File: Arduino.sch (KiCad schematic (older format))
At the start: 0 parts

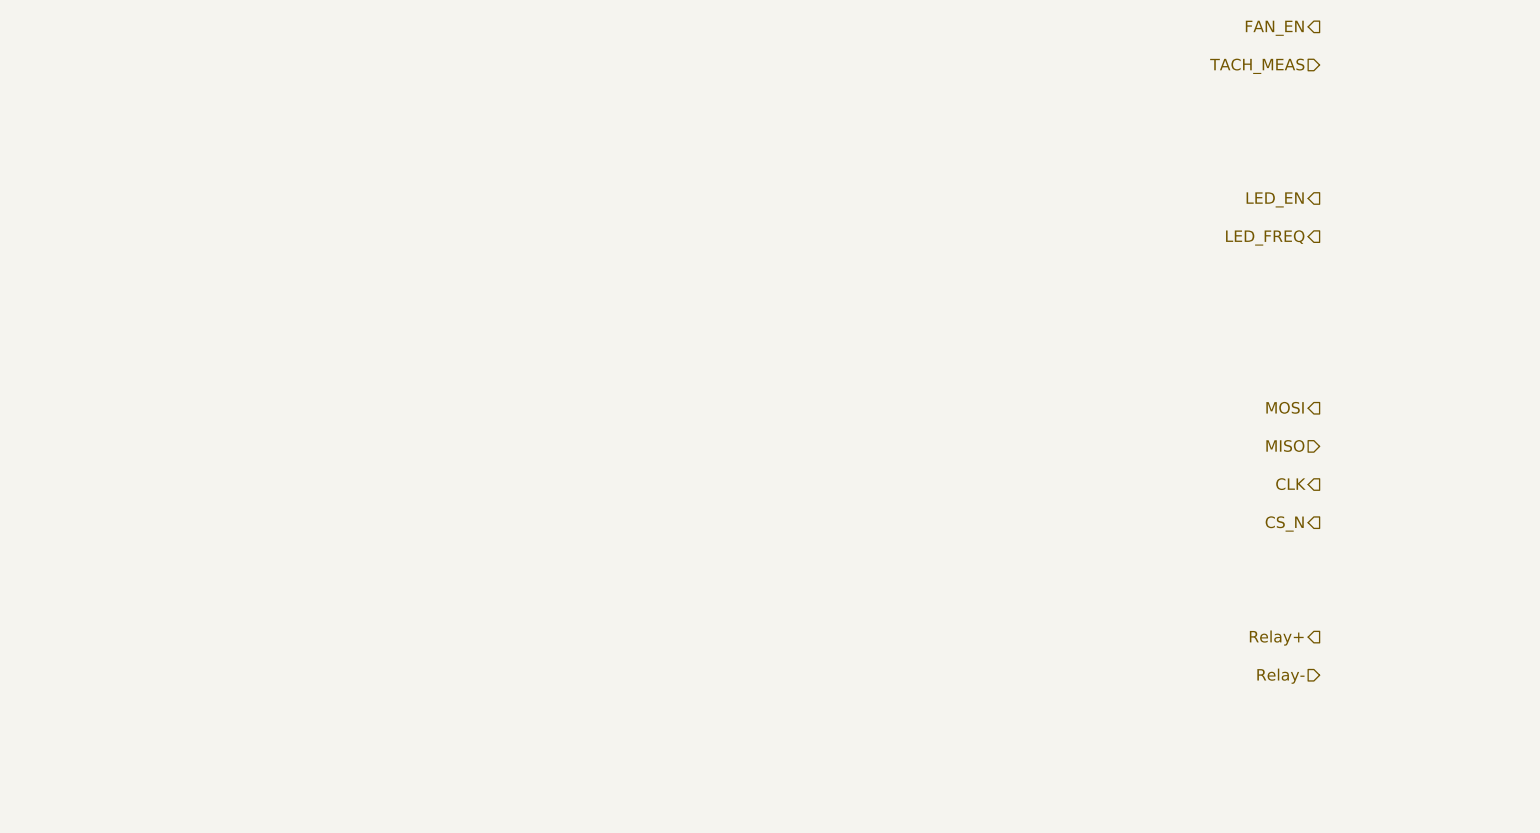
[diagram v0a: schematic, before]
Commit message: Added Arduino and top-level connections
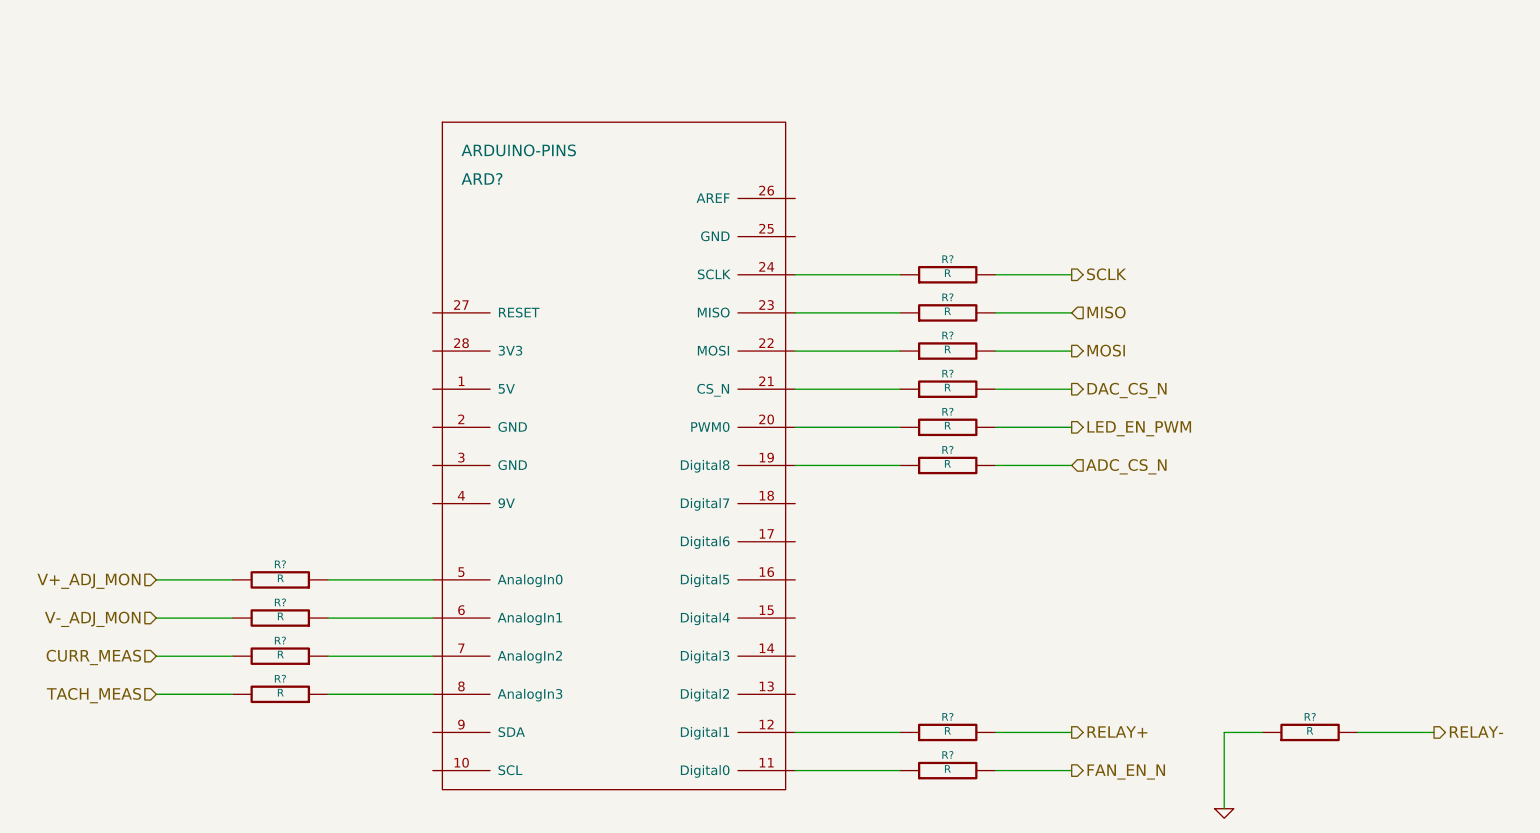
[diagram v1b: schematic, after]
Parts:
- added ARD?: ARDUINO-PINS, symbol ARDUINO-PINS
- added R? (x13): R, symbol R
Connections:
- net MISO: now also R?.2
- net MOSI: now also R?.2
- net TACH_MEAS: now also R?.2
- new net: ARD?.11 (Digital0), R?.1
- new net: ARD?.12 (Digital1), R?.1
- new net: ARD?.19 (Digital8), R?.1
- new net: ARD?.20 (PWM0), R?.1
- new net: ARD?.21 (CS_N), R?.1
- new net: ARD?.22 (MOSI), R?.1
- new net: ARD?.23 (MISO), R?.1
- new net: ARD?.24 (SCLK), R?.1
- new net: ARD?.5 (AnalogIn0), R?.1
- new net: ARD?.6 (AnalogIn1), R?.1
- new net: ARD?.7 (AnalogIn2), R?.1
- new net: ARD?.8 (AnalogIn3), R?.1
- new net ADC_CS_N: R?.2
- new net CURR_MEAS: R?.2
- new net DAC_CS_N: R?.2
- new net FAN_EN_N: R?.2
- new net GND: R?.1
- new net LED_EN_PWM: R?.2
- new net RELAY+: R?.2
- new net RELAY-: R?.2
- new net SCLK: R?.2
- new net V+_ADJ_MON: R?.2
- new net V-_ADJ_MON: R?.2

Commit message: Some cleanup/fixes on the top-level
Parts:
- added R? (x2): R, symbol R
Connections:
- net at ARD?.11 (Digital0): now also R?.1; no longer R?.1
- net at ARD?.18 (Digital7): now also R?.1
- net at ARD?.21 (CS_N): now also R?.1; no longer R?.1
- net at ARD?.4 (9V): now also R?.1
- net FAN_EN_N renamed FAN_PWM
- new net +12P: R?.2
- new net FAN_MODE: R?.2
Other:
- moved on the sheet: R?
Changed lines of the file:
@@
 $Descr A4 11693 8268
 encoding utf-8
-Sheet 7 9
+Sheet 9 9
 Title ""
 Date ""
@@
 Text HLabel 7100 2800 2    60   Output ~ 0
 SCLK
+Text HLabel 7100 4000 2    60   Output ~ 0
+DAC_CS_N
 Text HLabel 7100 3400 2    60   Output ~ 0
-DAC_CS_N
-Text HLabel 7100 5400 2    60   Output ~ 0
-FAN_EN_N
+FAN_PWM
 Text HLabel 2300 5000 0    60   Input ~ 0
 TACH_MEAS
@@
 L R R?
 U 1 1 52FC2526
-P 6450 5400
-F 0 "R?" V 6530 5400 40  0000 C CNN
-F 1 "R" V 6457 5401 40  0000 C CNN
-F 2 "" V 6380 5400 30  0000 C CNN
-F 3 "" H 6450 5400 30  0000 C CNN
-	1    6450 5400
-	0    -1   -1   0
-$EndComp
-Wire Wire Line
-	6700 5400 7100 5400
+P 6450 3400
+F 0 "R?" V 6530 3400 40  0000 C CNN
+F 1 "R" V 6457 3401 40  0000 C CNN
+F 2 "" V 6380 3400 30  0000 C CNN
+F 3 "" H 6450 3400 30  0000 C CNN
+	1    6450 3400
+	0    -1   -1   0
+$EndComp
+Wire Wire Line
+	6700 3400 7100 3400
 $Comp
 L R R?
@@
 	6200 5200 5650 5200
 Wire Wire Line
-	5650 5400 6200 5400
+	5650 3400 6200 3400
 $Comp
 L R R?
@@
 L R R?
 U 1 1 52FC406F
-P 6450 3400
-F 0 "R?" V 6530 3400 40  0000 C CNN
-F 1 "R" V 6457 3401 40  0000 C CNN
-F 2 "" V 6380 3400 30  0000 C CNN
-F 3 "" H 6450 3400 30  0000 C CNN
-	1    6450 3400
-	0    -1   -1   0
-$EndComp
-Wire Wire Line
-	6700 3400 7100 3400
+P 6450 4000
+F 0 "R?" V 6530 4000 40  0000 C CNN
+F 1 "R" V 6457 4001 40  0000 C CNN
+F 2 "" V 6380 4000 30  0000 C CNN
+F 3 "" H 6450 4000 30  0000 C CNN
+	1    6450 4000
+	0    -1   -1   0
+$EndComp
+Wire Wire Line
+	6700 4000 7100 4000
 $Comp
 L R R?
@@
 	6200 3200 5650 3200
 Wire Wire Line
-	5650 3400 6200 3400
+	5650 4000 6200 4000
 $Comp
 L R R?
@@
 Wire Wire Line
 	5650 3800 6200 3800
+Text HLabel 7100 5400 2    60   Input ~ 0
+FAN_MODE
+$Comp
+L R R?
+U 1 1 52FC1D68
+P 6450 5400
+F 0 "R?" V 6530 5400 40  0000 C CNN
+F 1 "R" V 6457 5401 40  0000 C CNN
+F 2 "" V 6380 5400 30  0000 C CNN
+F 3 "" H 6450 5400 30  0000 C CNN
+	1    6450 5400
+	0    -1   -1   0
+$EndComp
+Wire Wire Line
+	6700 5400 7100 5400
+Wire Wire Line
+	6200 5400 5650 5400
+$Comp
+L R R?
+U 1 1 52FC23F0
+P 2950 4000
+F 0 "R?" V 3030 4000 40  0000 C CNN
+F 1 "R" V 2957 4001 40  0000 C CNN
+F 2 "" V 2880 4000 30  0000 C CNN
+F 3 "" H 2950 4000 30  0000 C CNN
+	1    2950 4000
+	0    1    -1   0
+$EndComp
+Wire Wire Line
+	2700 4000 2300 4000
+Wire Wire Line
+	3200 4000 3750 4000
+$Comp
+L +12P #PWR?
+U 1 1 52FC23FA
+P 2300 3800
+F 0 "#PWR?" H 2300 3770 30  0001 C CNN
+F 1 "+12P" H 2300 3900 30  0000 C CNN
+F 2 "" H 2300 3800 60  0000 C CNN
+F 3 "" H 2300 3800 60  0000 C CNN
+	1    2300 3800
+	1    0    0    -1
+$EndComp
+Wire Wire Line
+	2300 4000 2300 3800
 $EndSCHEMATC

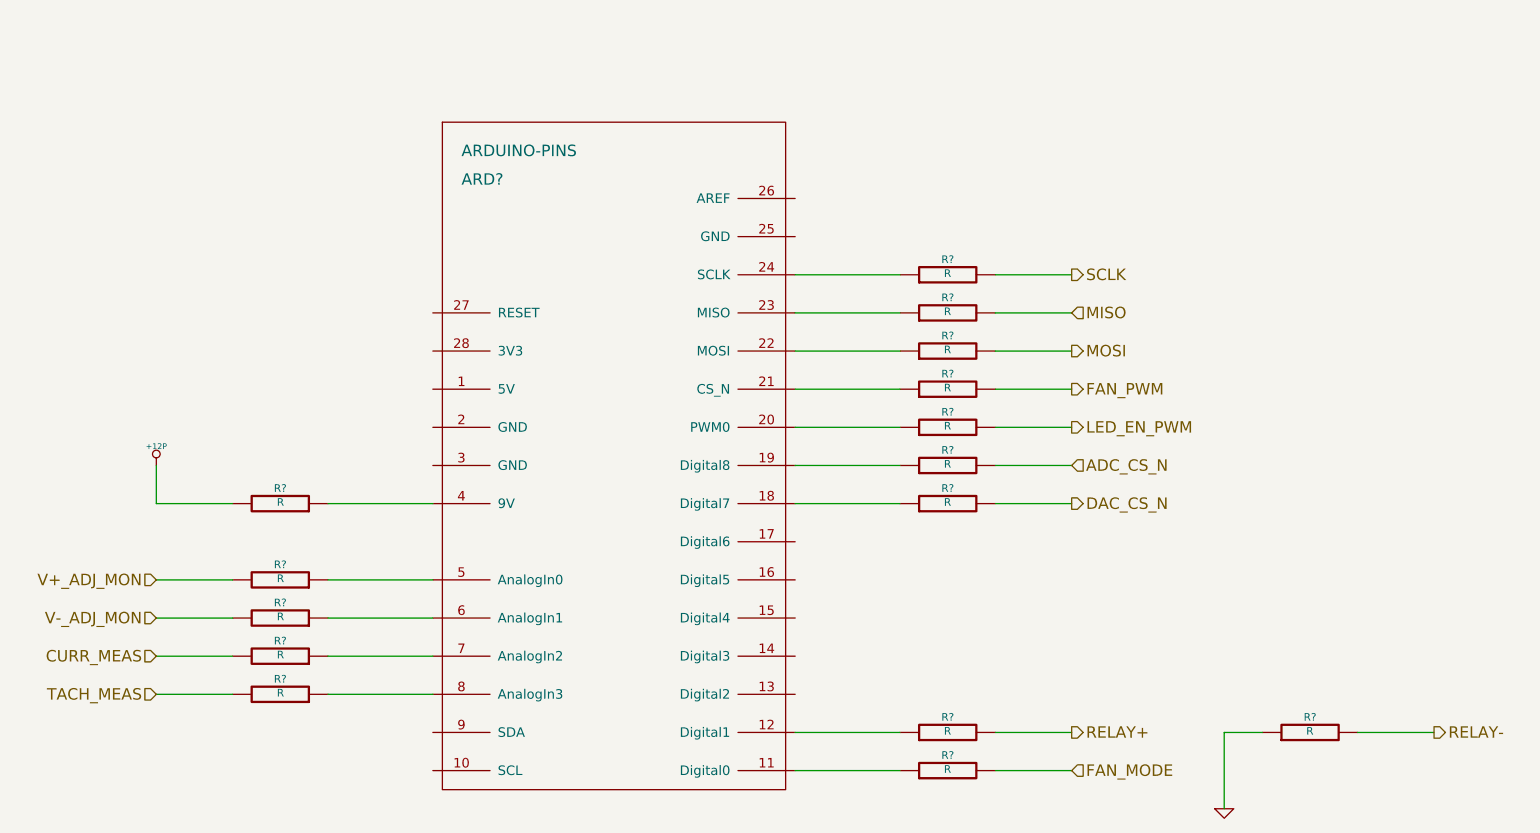
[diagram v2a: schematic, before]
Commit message: Added footprints for the relay module, preliminarily annotated schematic, relay components placed on PCB
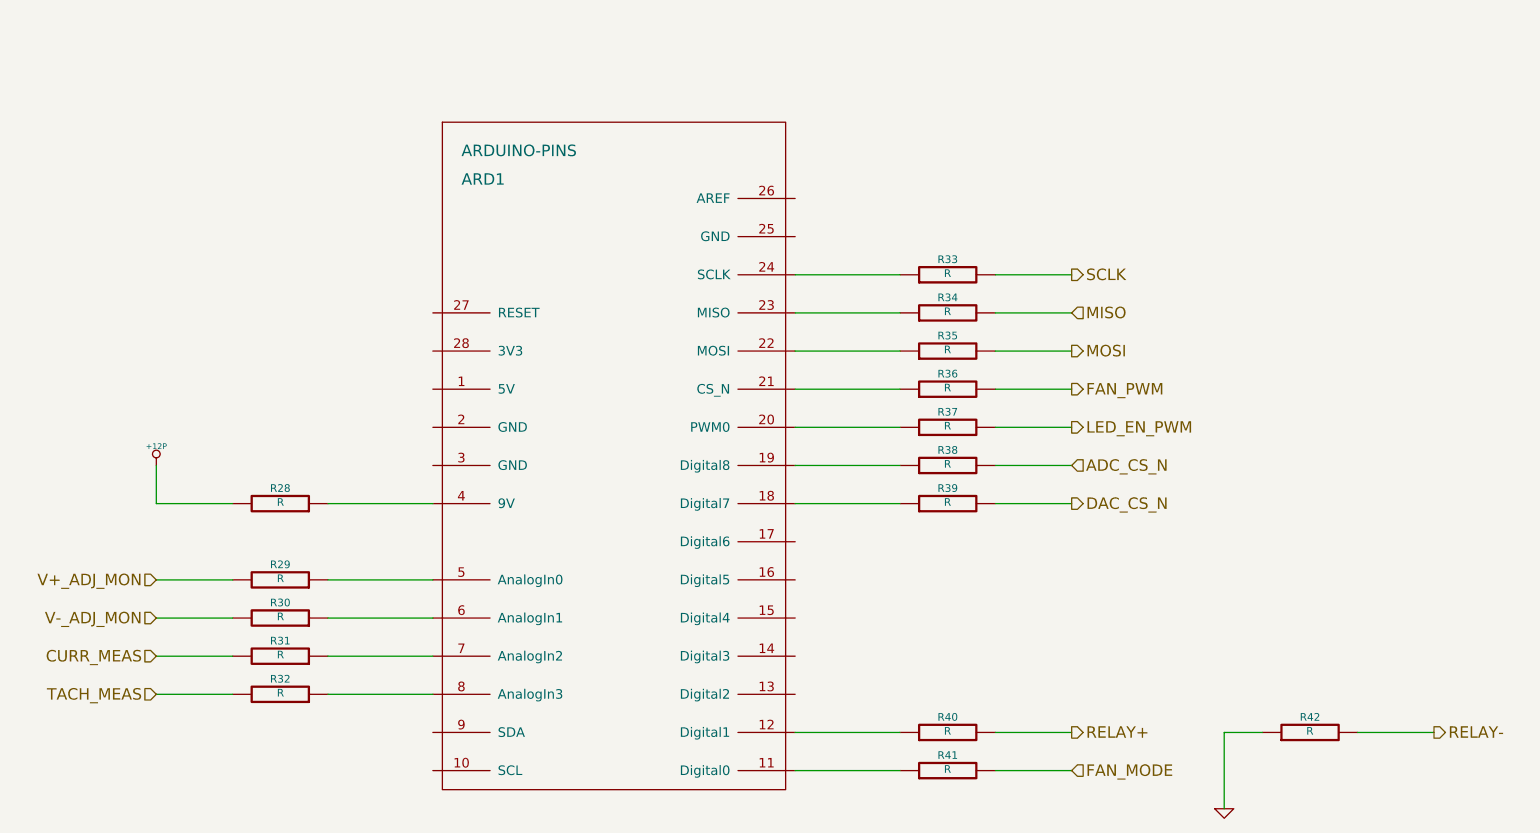
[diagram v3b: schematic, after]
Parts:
- gave numbers to parts that had none: 16
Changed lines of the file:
@@
 TACH_MEAS
 $Comp
-L ARDUINO-PINS ARD?
+L ARDUINO-PINS ARD1
 U 1 1 52FC2370
 P 4700 4100
-F 0 "ARD?" H 3900 5900 60  0000 L CNN
+F 0 "ARD1" H 3900 5900 60  0000 L CNN
 F 1 "ARDUINO-PINS" H 3900 6050 60  0000 L CNN
 F 2 "" H 4700 4100 60  0000 C CNN
@@
 CURR_MEAS
 $Comp
-L R R?
+L R R36
 U 1 1 52FC2526
 P 6450 3400
-F 0 "R?" V 6530 3400 40  0000 C CNN
+F 0 "R36" V 6530 3400 40  0000 C CNN
 F 1 "R" V 6457 3401 40  0000 C CNN
 F 2 "" V 6380 3400 30  0000 C CNN
@@
 	6700 3400 7100 3400
 $Comp
-L R R?
+L R R40
 U 1 1 52FC255A
 P 6450 5200
-F 0 "R?" V 6530 5200 40  0000 C CNN
+F 0 "R40" V 6530 5200 40  0000 C CNN
 F 1 "R" V 6457 5201 40  0000 C CNN
 F 2 "" V 6380 5200 30  0000 C CNN
@@
 	7900 5200 7900 5600
 $Comp
-L GND #PWR?
+L GND #PWR54
 U 1 1 52FC2D3A
 P 7900 5600
-F 0 "#PWR?" H 7900 5600 30  0001 C CNN
+F 0 "#PWR54" H 7900 5600 30  0001 C CNN
 F 1 "GND" H 7900 5530 30  0001 C CNN
 F 2 "" H 7900 5600 60  0000 C CNN
@@
 	5650 3400 6200 3400
 $Comp
-L R R?
+L R R32
 U 1 1 52FC2D75
 P 2950 5000
-F 0 "R?" V 3030 5000 40  0000 C CNN
+F 0 "R32" V 3030 5000 40  0000 C CNN
 F 1 "R" V 2957 5001 40  0000 C CNN
 F 2 "" V 2880 5000 30  0000 C CNN
@@
 	2700 5000 2300 5000
 $Comp
-L R R?
+L R R31
 U 1 1 52FC2D7C
 P 2950 4800
-F 0 "R?" V 3030 4800 40  0000 C CNN
+F 0 "R31" V 3030 4800 40  0000 C CNN
 F 1 "R" V 2957 4801 40  0000 C CNN
 F 2 "" V 2880 4800 30  0000 C CNN
@@
 V-_ADJ_MON
 $Comp
-L R R?
+L R R30
 U 1 1 52FC404F
 P 2950 4600
-F 0 "R?" V 3030 4600 40  0000 C CNN
+F 0 "R30" V 3030 4600 40  0000 C CNN
 F 1 "R" V 2957 4601 40  0000 C CNN
 F 2 "" V 2880 4600 30  0000 C CNN
@@
 	2700 4600 2300 4600
 $Comp
-L R R?
+L R R29
 U 1 1 52FC4056
 P 2950 4400
-F 0 "R?" V 3030 4400 40  0000 C CNN
+F 0 "R29" V 3030 4400 40  0000 C CNN
 F 1 "R" V 2957 4401 40  0000 C CNN
 F 2 "" V 2880 4400 30  0000 C CNN
@@
 	3750 4600 3200 4600
 $Comp
-L R R?
+L R R34
 U 1 1 52FC405F
 P 6450 3000
-F 0 "R?" V 6530 3000 40  0000 C CNN
+F 0 "R34" V 6530 3000 40  0000 C CNN
 F 1 "R" V 6457 3001 40  0000 C CNN
 F 2 "" V 6380 3000 30  0000 C CNN
@@
 	6700 3000 7100 3000
 $Comp
-L R R?
+L R R33
 U 1 1 52FC4066
 P 6450 2800
-F 0 "R?" V 6530 2800 40  0000 C CNN
+F 0 "R33" V 6530 2800 40  0000 C CNN
 F 1 "R" V 6457 2801 40  0000 C CNN
 F 2 "" V 6380 2800 30  0000 C CNN
@@
 	5650 3000 6200 3000
 $Comp
-L R R?
+L R R39
 U 1 1 52FC406F
 P 6450 4000
-F 0 "R?" V 6530 4000 40  0000 C CNN
+F 0 "R39" V 6530 4000 40  0000 C CNN
 F 1 "R" V 6457 4001 40  0000 C CNN
 F 2 "" V 6380 4000 30  0000 C CNN
@@
 	6700 4000 7100 4000
 $Comp
-L R R?
+L R R35
 U 1 1 52FC4076
 P 6450 3200
-F 0 "R?" V 6530 3200 40  0000 C CNN
+F 0 "R35" V 6530 3200 40  0000 C CNN
 F 1 "R" V 6457 3201 40  0000 C CNN
 F 2 "" V 6380 3200 30  0000 C CNN
@@
 	5650 4000 6200 4000
 $Comp
-L R R?
+L R R42
 U 1 1 52FC4081
 P 8350 5200
-F 0 "R?" V 8430 5200 40  0000 C CNN
+F 0 "R42" V 8430 5200 40  0000 C CNN
 F 1 "R" V 8357 5201 40  0000 C CNN
 F 2 "" V 8280 5200 30  0000 C CNN
@@
 LED_EN_PWM
 $Comp
-L R R?
+L R R37
 U 1 1 52FC408C
 P 6450 3600
-F 0 "R?" V 6530 3600 40  0000 C CNN
+F 0 "R37" V 6530 3600 40  0000 C CNN
 F 1 "R" V 6457 3601 40  0000 C CNN
 F 2 "" V 6380 3600 30  0000 C CNN
@@
 ADC_CS_N
 $Comp
-L R R?
+L R R38
 U 1 1 52FDBDB3
 P 6450 3800
-F 0 "R?" V 6530 3800 40  0000 C CNN
+F 0 "R38" V 6530 3800 40  0000 C CNN
 F 1 "R" V 6457 3801 40  0000 C CNN
 F 2 "" V 6380 3800 30  0000 C CNN
@@
 FAN_MODE
 $Comp
-L R R?
+L R R41
 U 1 1 52FC1D68
 P 6450 5400
-F 0 "R?" V 6530 5400 40  0000 C CNN
+F 0 "R41" V 6530 5400 40  0000 C CNN
 F 1 "R" V 6457 5401 40  0000 C CNN
 F 2 "" V 6380 5400 30  0000 C CNN
@@
 	6200 5400 5650 5400
 $Comp
-L R R?
+L R R28
 U 1 1 52FC23F0
 P 2950 4000
-F 0 "R?" V 3030 4000 40  0000 C CNN
+F 0 "R28" V 3030 4000 40  0000 C CNN
 F 1 "R" V 2957 4001 40  0000 C CNN
 F 2 "" V 2880 4000 30  0000 C CNN
@@
 	3200 4000 3750 4000
 $Comp
-L +12P #PWR?
+L +12P #PWR53
 U 1 1 52FC23FA
 P 2300 3800
-F 0 "#PWR?" H 2300 3770 30  0001 C CNN
+F 0 "#PWR53" H 2300 3770 30  0001 C CNN
 F 1 "+12P" H 2300 3900 30  0000 C CNN
 F 2 "" H 2300 3800 60  0000 C CNN

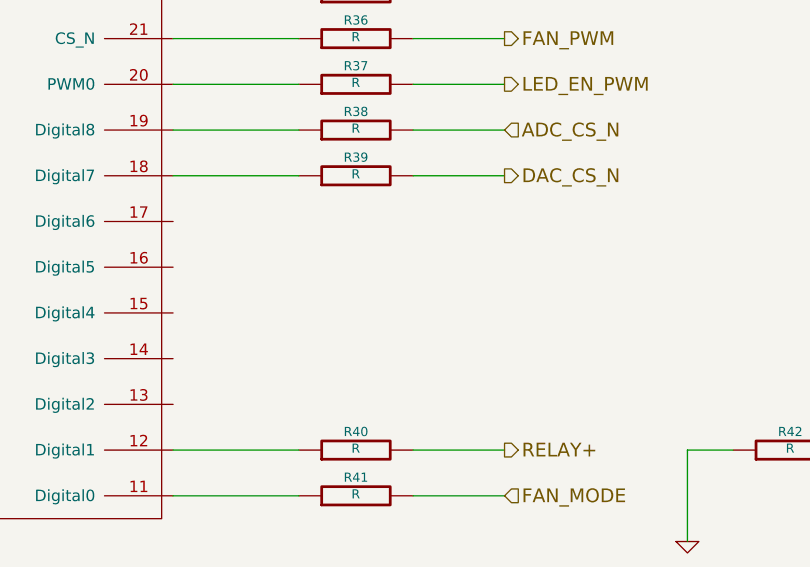
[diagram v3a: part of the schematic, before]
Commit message: Associated and placed the thermocouple module
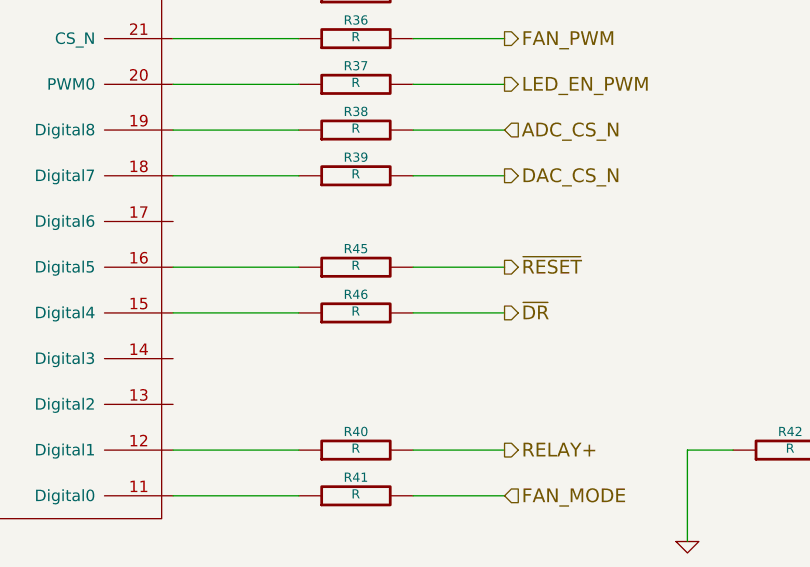
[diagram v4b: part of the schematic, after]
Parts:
- added R45, R46: R, symbol R
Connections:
- net at ARD1.15 (Digital4): now also R46.1
- net at ARD1.16 (Digital5): now also R45.1
- new net ~DR: R46.2
- new net ~RESET: R45.2
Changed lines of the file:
@@
 	7900 5200 7900 5600
 $Comp
-L GND #PWR54
+L GND #PWR61
 U 1 1 52FC2D3A
 P 7900 5600
-F 0 "#PWR54" H 7900 5600 30  0001 C CNN
+F 0 "#PWR61" H 7900 5600 30  0001 C CNN
 F 1 "GND" H 7900 5530 30  0001 C CNN
 F 2 "" H 7900 5600 60  0000 C CNN
@@
 	3200 4000 3750 4000
 $Comp
-L +12P #PWR53
+L +12P #PWR60
 U 1 1 52FC23FA
 P 2300 3800
-F 0 "#PWR53" H 2300 3770 30  0001 C CNN
+F 0 "#PWR60" H 2300 3770 30  0001 C CNN
 F 1 "+12P" H 2300 3900 30  0000 C CNN
 F 2 "" H 2300 3800 60  0000 C CNN
@@
 Wire Wire Line
 	2300 4000 2300 3800
+Text HLabel 7100 4400 2    60   Output ~ 0
+~RESET
+$Comp
+L R R45
+U 1 1 5305743E
+P 6450 4400
+F 0 "R45" V 6530 4400 40  0000 C CNN
+F 1 "R" V 6457 4401 40  0000 C CNN
+F 2 "" V 6380 4400 30  0000 C CNN
+F 3 "" H 6450 4400 30  0000 C CNN
+	1    6450 4400
+	0    -1   -1   0
+$EndComp
+Wire Wire Line
+	6700 4400 7100 4400
+Wire Wire Line
+	5650 4400 6200 4400
+Text HLabel 7100 4600 2    60   Output ~ 0
+~DR
+$Comp
+L R R46
+U 1 1 53057447
+P 6450 4600
+F 0 "R46" V 6530 4600 40  0000 C CNN
+F 1 "R" V 6457 4601 40  0000 C CNN
+F 2 "" V 6380 4600 30  0000 C CNN
+F 3 "" H 6450 4600 30  0000 C CNN
+	1    6450 4600
+	0    -1   -1   0
+$EndComp
+Wire Wire Line
+	6700 4600 7100 4600
+Wire Wire Line
+	5650 4600 6200 4600
 $EndSCHEMATC
